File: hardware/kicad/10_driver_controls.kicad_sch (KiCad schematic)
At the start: 38 parts, among them J1001 DRIVER_CONTROLS, U1001 PC817 (safety-loop sense)

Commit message: sem-motor-controller v0.3: vehicle-interface provenance, transport-neutral core, clock trees, schematic checks
Provenance: the Cornell repositories are reference projects. Every place
that treated CHUDS / CAN FD / its VCU / 40 MHz as our vehicle is relabelled
or corrected (docs/PROVENANCE_AUDIT.md); the v0.2 checkpoint is preserved
with an errata banner.

Firmware: the core is transport-neutral (mc_core_on_msg_rx /
mc_core_msg_tx_poll / mc_core_on_link_state). CAN is one binding
(src/transport/mc_can_binding.c) whose 64-identifier block base is the new
calibration parameter supervision.can_id_base (id 164, rule 40, null in the
unconfigured config). ADR-0012. Tests: block relocation with a full ECO
engagement at 0x500, neutral API, rule-40 C/Python parity.

Clocking: tools/clock_tree.py evaluates 28 complete clock trees x 4 bus
cases from ST register widths and HAL ranges; the v0.2 "40 MHz required"
claim is withdrawn and the crystal is unselected until the bus is known.

Schematic: INA228 pins renumbered (KiCad-library cross-check, secondary);
DRV8353S stays an explicit placeholder; crystal unselected; PWR_FLAGs added
after a new pin-type check (not an ERC) found 6 undriven-rail errors.
Real KiCad ERC not run (KiCad 7 has no CLI ERC; tools/run_kicad_erc.sh).

Telematics: combined architecture with the STM32U575 / CAN 2.0B / LTE-MQTT
proposal (supervisor and CSIA placement, torque-request and driver-
authorization paths, pit/cloud outside the control chain), interface
difference table, generated DBC, logging-capacity and auxiliary-power
budget. Validation language separates command ceilings, envelope ramp,
phase current and battery current. CSIA: component attribution and a
next-evaluation plan; frozen results unchanged, nothing re-run.

Verified on the host: ctest 6/6 (4,006 checks), pytest 199 passed,
ARM core build 0 warnings, generators current, KiCad connectivity 0
problems. Nothing on hardware.

Co-Authored-By: Claude Opus 5.5 <noreply@anthropic.com>
Claude-Ses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
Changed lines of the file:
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@@
     (pin "2")
   )
-  (symbol (lib_id "Device:R") (at 248.92000000000002 66.04 0) (unit 1)
-    (in_bom yes) (on_board yes)
-    (property "Reference" "R1002" (id 0) (at 248.92000000000002 60.96000000000001 0)
-      (effects (font (size 1.27 1.27)))
-    )
-    (property "Value" "18k" (id 1) (at 248.92000000000002 71.12 0)
-      (effects (font (size 1.27 1.27)))
-    )
-    (property "Footprint" "" (id 2) (at 248.92000000000002 66.04 0)
-      (effects (font (size 1.27 1.27)) hide)
-    )
-    (property "Datasheet" "" (id 3) (at 248.92000000000002 66.04 0)
-      (effects (font (size 1.27 1.27)) hide)
-    )
-    (property "Status" "design value" (id 4) (at 248.92000000000002 66.04 0)
-      (effects (font (size 1.27 1.27)) hide)
-    )
-    (property "Rating_basis" "5 V -> 3.21 V" (id 5) (at 248.92000000000002 66.04 0)
+  (symbol (lib_id "Device:R") (at 248.92 66.04 0) (unit 1)
+    (in_bom yes) (on_board yes)
+    (property "Reference" "R1002" (id 0) (at 248.92 60.96000000000001 0)
+      (effects (font (size 1.27 1.27)))
+    )
+    (property "Value" "18k" (id 1) (at 248.92 71.12 0)
+      (effects (font (size 1.27 1.27)))
+    )
+    (property "Footprint" "" (id 2) (at 248.92 66.04 0)
+      (effects (font (size 1.27 1.27)) hide)
+    )
+    (property "Datasheet" "" (id 3) (at 248.92 66.04 0)
+      (effects (font (size 1.27 1.27)) hide)
+    )
+    (property "Status" "design value" (id 4) (at 248.92 66.04 0)
+      (effects (font (size 1.27 1.27)) hide)
+    )
+    (property "Rating_basis" "5 V -> 3.21 V" (id 5) (at 248.92 66.04 0)
       (effects (font (size 1.27 1.27)) hide)
     )
@@
     (pin "2")
   )
-  (symbol (lib_id "Device:C") (at 370.84000000000003 66.04 0) (unit 1)
-    (in_bom yes) (on_board yes)
-    (property "Reference" "C1001" (id 0) (at 370.84000000000003 60.96000000000001 0)
-      (effects (font (size 1.27 1.27)))
-    )
-    (property "Value" "100nF" (id 1) (at 370.84000000000003 71.12 0)
-      (effects (font (size 1.27 1.27)))
-    )
-    (property "Footprint" "" (id 2) (at 370.84000000000003 66.04 0)
-      (effects (font (size 1.27 1.27)) hide)
-    )
-    (property "Datasheet" "" (id 3) (at 370.84000000000003 66.04 0)
-      (effects (font (size 1.27 1.27)) hide)
-    )
-    (property "Status" "design value" (id 4) (at 370.84000000000003 66.04 0)
+  (symbol (lib_id "Device:C") (at 370.84 66.04 0) (unit 1)
+    (in_bom yes) (on_board yes)
+    (property "Reference" "C1001" (id 0) (at 370.84 60.96000000000001 0)
+      (effects (font (size 1.27 1.27)))
+    )
+    (property "Value" "100nF" (id 1) (at 370.84 71.12 0)
+      (effects (font (size 1.27 1.27)))
+    )
+    (property "Footprint" "" (id 2) (at 370.84 66.04 0)
+      (effects (font (size 1.27 1.27)) hide)
+    )
+    (property "Datasheet" "" (id 3) (at 370.84 66.04 0)
+      (effects (font (size 1.27 1.27)) hide)
+    )
+    (property "Status" "design value" (id 4) (at 370.84 66.04 0)
       (effects (font (size 1.27 1.27)) hide)
     )
@@
     (pin "2")
   )
-  (symbol (lib_id "Device:R") (at 248.92000000000002 119.38 0) (unit 1)
-    (in_bom yes) (on_board yes)
-    (property "Reference" "R1008" (id 0) (at 248.92000000000002 114.3 0)
-      (effects (font (size 1.27 1.27)))
-    )
-    (property "Value" "1k" (id 1) (at 248.92000000000002 124.46 0)
-      (effects (font (size 1.27 1.27)))
-    )
-    (property "Footprint" "" (id 2) (at 248.92000000000002 119.38 0)
-      (effects (font (size 1.27 1.27)) hide)
-    )
-    (property "Datasheet" "" (id 3) (at 248.92000000000002 119.38 0)
-      (effects (font (size 1.27 1.27)) hide)
-    )
-    (property "Status" "design value" (id 4) (at 248.92000000000002 119.38 0)
+  (symbol (lib_id "Device:R") (at 248.92 119.38 0) (unit 1)
+    (in_bom yes) (on_board yes)
+    (property "Reference" "R1008" (id 0) (at 248.92 114.3 0)
+      (effects (font (size 1.27 1.27)))
+    )
+    (property "Value" "1k" (id 1) (at 248.92 124.46 0)
+      (effects (font (size 1.27 1.27)))
+    )
+    (property "Footprint" "" (id 2) (at 248.92 119.38 0)
+      (effects (font (size 1.27 1.27)) hide)
+    )
+    (property "Datasheet" "" (id 3) (at 248.92 119.38 0)
+      (effects (font (size 1.27 1.27)) hide)
+    )
+    (property "Status" "design value" (id 4) (at 248.92 119.38 0)
       (effects (font (size 1.27 1.27)) hide)
     )
@@
     (pin "2")
   )
-  (symbol (lib_id "Device:R") (at 71.12 248.92000000000002 0) (unit 1)
-    (in_bom yes) (on_board yes)
-    (property "Reference" "R1020" (id 0) (at 71.12 243.84 0)
-      (effects (font (size 1.27 1.27)))
-    )
-    (property "Value" "10k" (id 1) (at 71.12 254.00000000000003 0)
-      (effects (font (size 1.27 1.27)))
-    )
-    (property "Footprint" "" (id 2) (at 71.12 248.92000000000002 0)
-      (effects (font (size 1.27 1.27)) hide)
-    )
-    (property "Datasheet" "" (id 3) (at 71.12 248.92000000000002 0)
-      (effects (font (size 1.27 1.27)) hide)
-    )
-    (property "Status" "design value" (id 4) (at 71.12 248.92000000000002 0)
-      (effects (font (size 1.27 1.27)) hide)
-    )
-    (property "Rating_basis" "HW_PERMIT low unless the loop is energised" (id 5) (at 71.12 248.92000000000002 0)
-      (effects (font (size 1.27 1.27)) hide)
-    )
-    (pin "1")
-    (pin "2")
-  )
-  (symbol (lib_id "Device:C") (at 129.54 248.92000000000002 0) (unit 1)
-    (in_bom yes) (on_board yes)
-    (property "Reference" "C1009" (id 0) (at 129.54 243.84 0)
-      (effects (font (size 1.27 1.27)))
-    )
-    (property "Value" "1nF" (id 1) (at 129.54 254.00000000000003 0)
-      (effects (font (size 1.27 1.27)))
-    )
-    (property "Footprint" "" (id 2) (at 129.54 248.92000000000002 0)
-      (effects (font (size 1.27 1.27)) hide)
-    )
-    (property "Datasheet" "" (id 3) (at 129.54 248.92000000000002 0)
-      (effects (font (size 1.27 1.27)) hide)
-    )
-    (property "Status" "design value" (id 4) (at 129.54 248.92000000000002 0)
-      (effects (font (size 1.27 1.27)) hide)
-    )
+  (symbol (lib_id "Device:R") (at 71.12 248.92 0) (unit 1)
+    (in_bom yes) (on_board yes)
+    (property "Reference" "R1020" (id 0) (at 71.12 243.83999999999997 0)
+      (effects (font (size 1.27 1.27)))
+    )
+    (property "Value" "10k" (id 1) (at 71.12 254.0 0)
+      (effects (font (size 1.27 1.27)))
+    )
+    (property "Footprint" "" (id 2) (at 71.12 248.92 0)
+      (effects (font (size 1.27 1.27)) hide)
+    )
+    (property "Datasheet" "" (id 3) (at 71.12 248.92 0)
+      (effects (font (size 1.27 1.27)) hide)
+    )
+    (property "Status" "design value" (id 4) (at 71.12 248.92 0)
+      (effects (font (size 1.27 1.27)) hide)
+    )
+    (property "Rating_basis" "HW_PERMIT low unless the loop is energised" (id 5) (at 71.12 248.92 0)
+      (effects (font (size 1.27 1.27)) hide)
+    )
+    (pin "1")
+    (pin "2")
+  )
+  (symbol (lib_id "Device:C") (at 129.54 248.92 0) (unit 1)
+    (in_bom yes) (on_board yes)
+    (property "Reference" "C1009" (id 0) (at 129.54 243.83999999999997 0)
+      (effects (font (size 1.27 1.27)))
+    )
+    (property "Value" "1nF" (id 1) (at 129.54 254.0 0)
+      (effects (font (size 1.27 1.27)))
+    )
+    (property "Footprint" "" (id 2) (at 129.54 248.92 0)
+      (effects (font (size 1.27 1.27)) hide)
+    )
+    (property "Datasheet" "" (id 3) (at 129.54 248.92 0)
+      (effects (font (size 1.27 1.27)) hide)
+    )
+    (property "Status" "design value" (id 4) (at 129.54 248.92 0)
+      (effects (font (size 1.27 1.27)) hide)
+    )

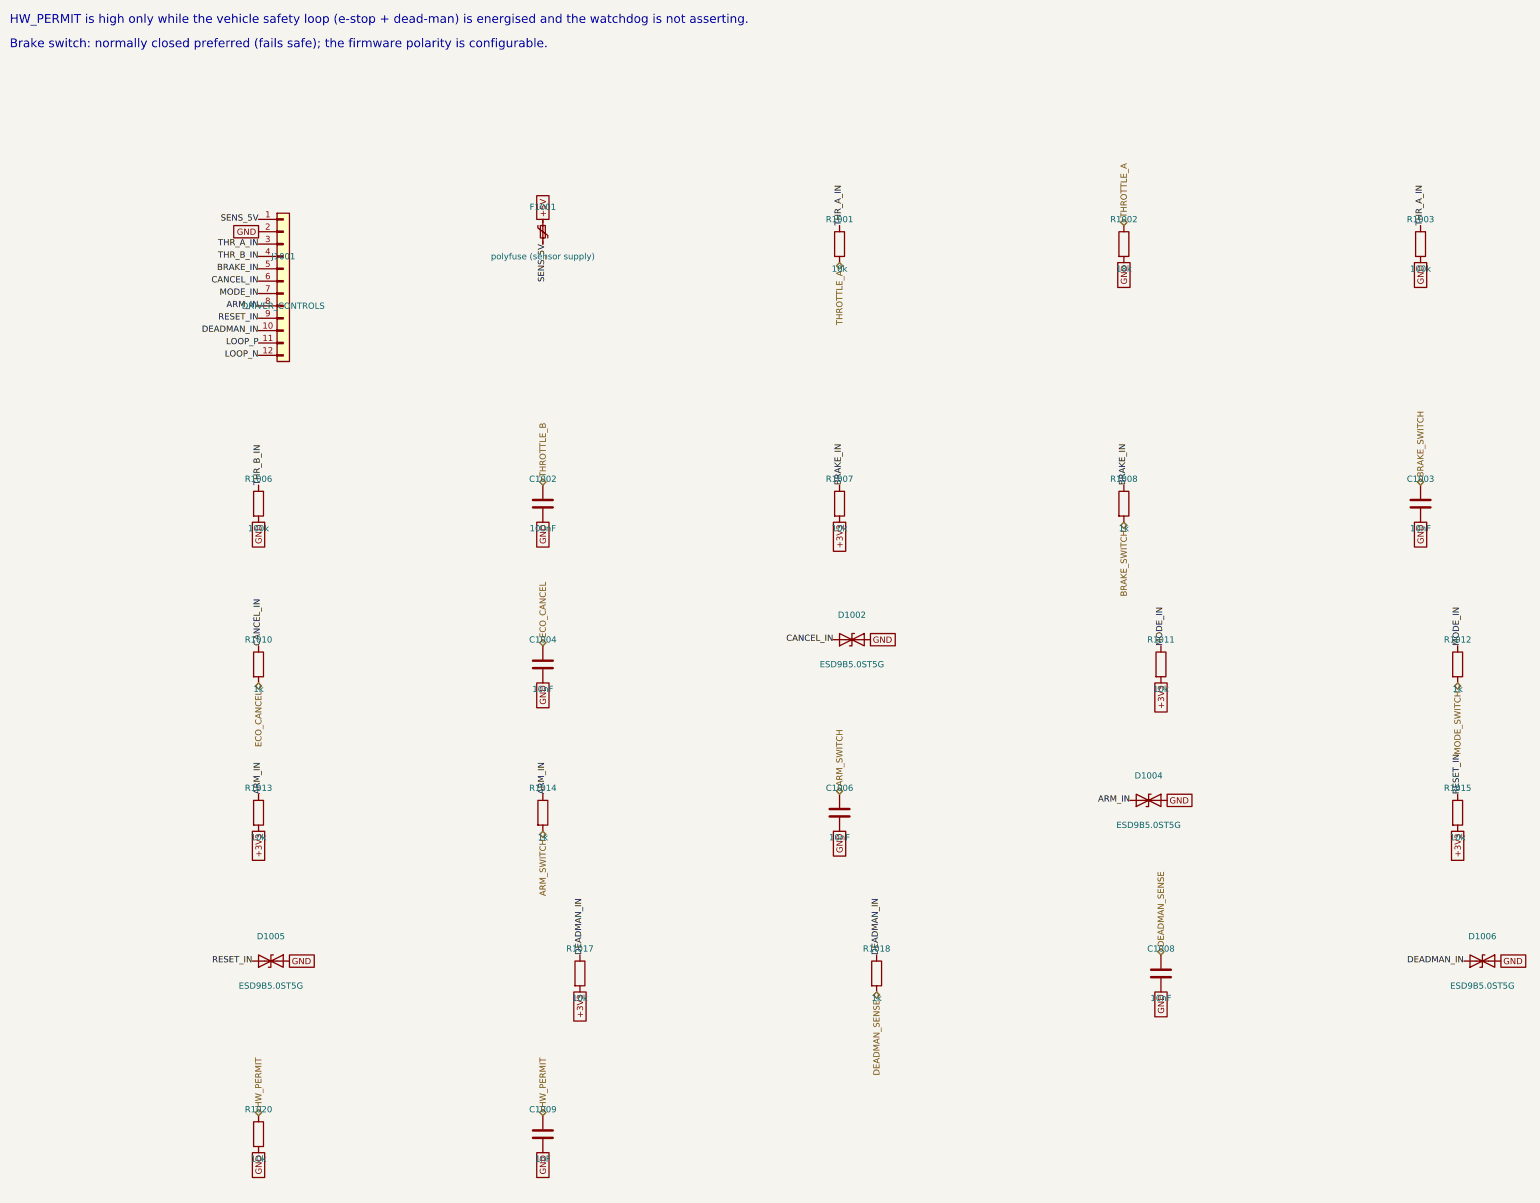
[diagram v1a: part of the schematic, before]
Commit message: hardware: design review, OV comparator hysteresis fix, test points, KiCad 8.0.9 libraries
hardware/review/DESIGN_REVIEW.md reviews the draft item by item (gate
driver, MOSFETs, DC link, current sensing, hardware overcurrent,
over/undervoltage, temperature, precharge, enable defaults and
watchdog, emergency interface, DC-DC, CAN, clock, debug and test
points) with an evidence level per statement, and records what each
open item needs.

Schematic changes that need no vehicle data:
- the over-voltage comparator's hysteresis resistor went straight onto
  the TL431 node, whose low impedance made the hysteresis undefined;
  the + input is now fed through 10 k and 390 k from the output sets
  -2.5 % / +0.8 % around the reference;
- the TL431 bias is 470 ohm (1.7 mA) instead of 1 k (0.8 mA), above
  its minimum cathode current (recalled; to confirm in the datasheet);
- the six pull-downs on the gate-signal inputs are fitted until the
  driver's own pull-downs are verified;
- 21 test points for the signals the acceptance procedures probe.
Connectivity: 136 intended nets, 0 problems; pin types 0 findings;
consistency 14 PASS, 4 OPEN.

The nine KiCad 8.0.9 ERC warnings were each compared with the library:
PWR_FLAG pin name, TL431 drawing, STM32G474 symbol geometry and the
NUP2105L datasheet URL changed between the 7.0.11 library the
schematic embedded and 8.0.9; no pin number, connected name, type or
net changed. The schematic is now generated from a pinned, SHA-256
checked copy of the 8.0.9 libraries (tools/fetch_kicad_symbols.py),
which the ERC also reads; KiCad 8's (hide yes) spelling is converted
for kiutils so no field becomes visible. Both CI jobs use KiCad 8.

Firmware: the brake switch type is a calibration value; a separate
bench image (semmc_stm32g474_pwmtest) switches the gate signals at
fixed duties with DRV_ENABLE held low for acceptance stage 4; g_bench
also reports the input states.

Co-Authored-By: Claude Opus 5.5 <noreply@anthropic.com>
Claude-Session: https:/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
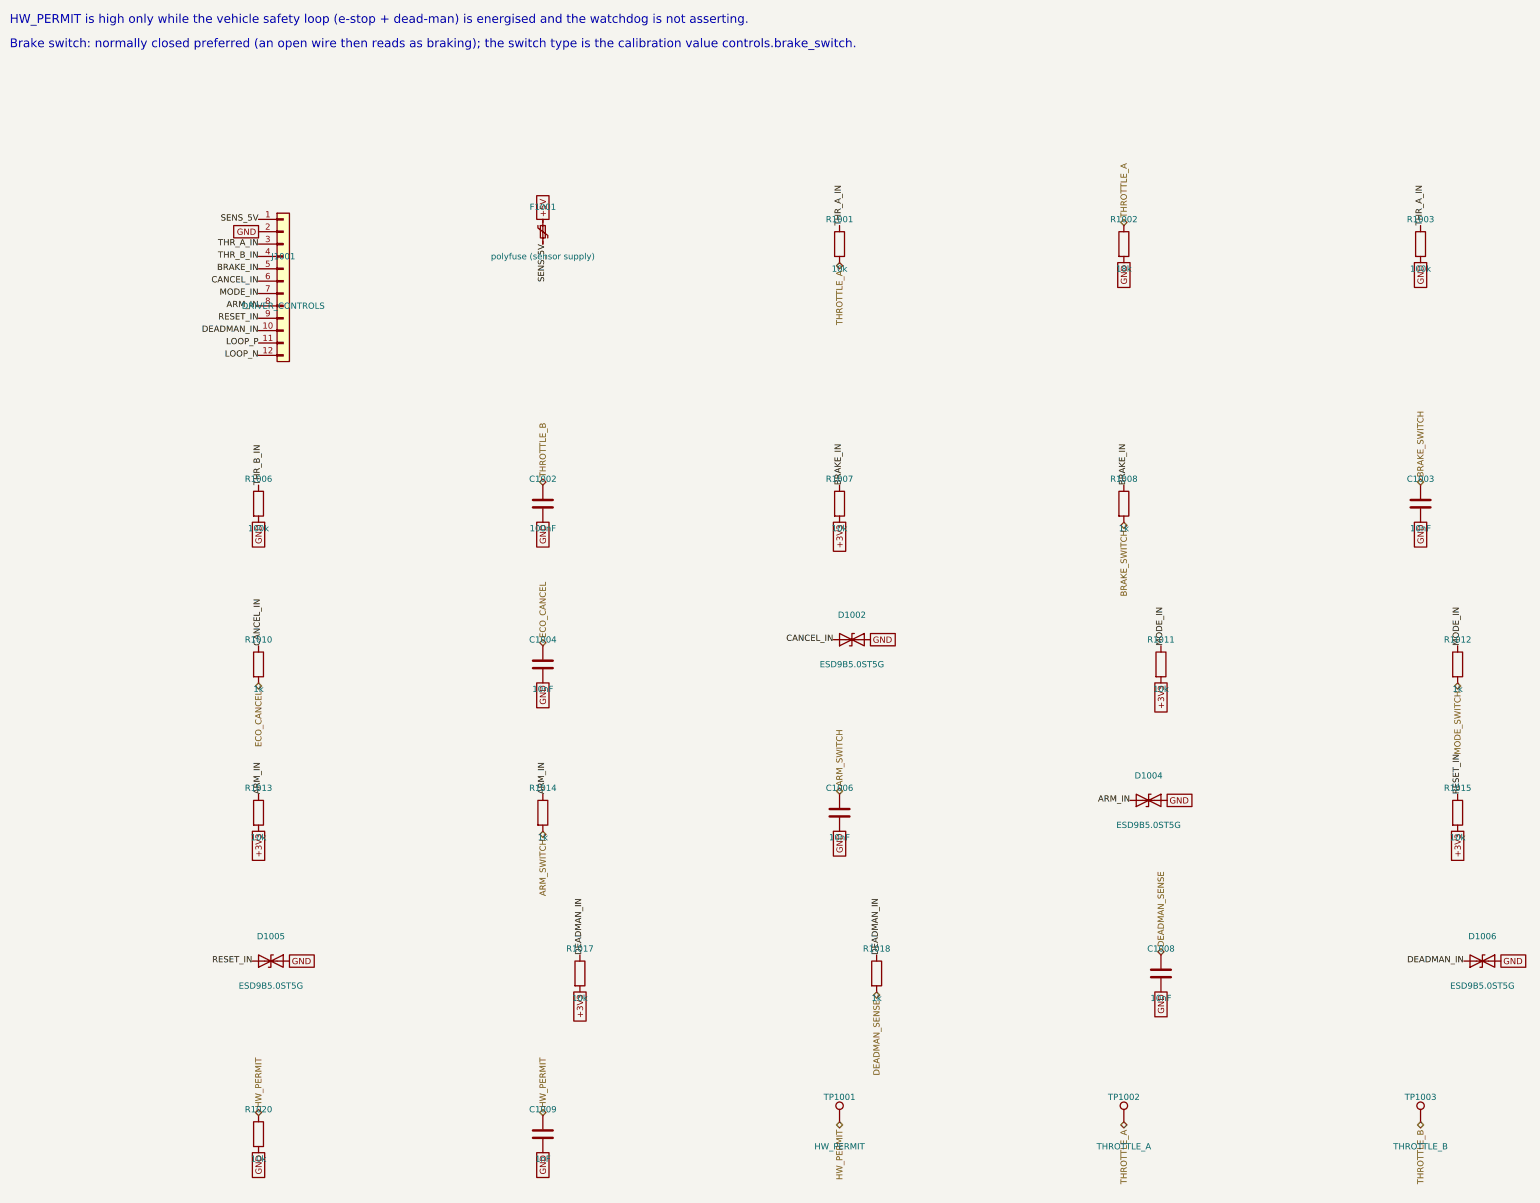
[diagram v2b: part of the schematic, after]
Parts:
- added TP1001: HW_PERMIT, symbol Connector:TestPoint
- added TP1002: THROTTLE_A, symbol Connector:TestPoint
- added TP1003: THROTTLE_B, symbol Connector:TestPoint
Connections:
- net HW_PERMIT: now also TP1001.1
- net THROTTLE_A: now also TP1002.1
- net THROTTLE_B: now also TP1003.1
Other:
- note added: "Brake switch: normally closed preferred (an open wire then reads as braking); the switch type is the calibration value controls.brake_switch."
- note removed: "Brake switch: normally closed preferred (fails safe); the firmware polarity is configurable."
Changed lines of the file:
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@@
     (effects (font (size 1.8 1.8)) (justify left))
   )
-  (text "Brake switch: normally closed preferred (fails safe); the firmware polarity is configurable."
+  (text "Brake switch: normally closed preferred (an open wire then reads as braking); the switch type is the calibration value controls.brake_switch."
     (at 20.0 25.0 0)
     (effects (font (size 1.8 1.8)) (justify left))
@@
   (hierarchical_label "HW_PERMIT" (shape bidirectional) (at 129.54 245.11 90)
     (effects (font (size 1.27 1.27)) (justify left))
+  )
+  (hierarchical_label "HW_PERMIT" (shape bidirectional) (at 190.5 246.38 270)
+    (effects (font (size 1.27 1.27)) (justify right))
+  )
+  (hierarchical_label "THROTTLE_A" (shape bidirectional) (at 248.92 246.38 270)
+    (effects (font (size 1.27 1.27)) (justify right))
+  )
+  (hierarchical_label "THROTTLE_B" (shape bidirectional) (at 309.88 246.38 270)
+    (effects (font (size 1.27 1.27)) (justify right))
   )
   (symbol (lib_id "Connector_Generic:Conn_01x12") (at 76.2 73.66 0) (unit 1)
@@
     (pin "2")
   )
+  (symbol (lib_id "Connector:TestPoint") (at 190.5 246.38 0) (unit 1)
+    (in_bom yes) (on_board yes)
+    (property "Reference" "TP1001" (id 0) (at 190.5 241.29999999999998 0)
+      (effects (font (size 1.27 1.27)))
+    )
+    (property "Value" "HW_PERMIT" (id 1) (at 190.5 251.46 0)
+      (effects (font (size 1.27 1.27)))
+    )
+    (property "Footprint" "" (id 2) (at 190.5 246.38 0)
+      (effects (font (size 1.27 1.27)) hide)
+    )
+    (property "Datasheet" "" (id 3) (at 190.5 246.38 0)
+      (effects (font (size 1.27 1.27)) hide)
+    )
+    (property "Status" "bench test point" (id 4) (at 190.5 246.38 0)
+      (effects (font (size 1.27 1.27)) hide)
+    )
+    (pin "1")
+  )
+  (symbol (lib_id "Connector:TestPoint") (at 248.92 246.38 0) (unit 1)
+    (in_bom yes) (on_board yes)
+    (property "Reference" "TP1002" (id 0) (at 248.92 241.29999999999998 0)
+      (effects (font (size 1.27 1.27)))
+    )
+    (property "Value" "THROTTLE_A" (id 1) (at 248.92 251.46 0)
+      (effects (font (size 1.27 1.27)))
+    )
+    (property "Footprint" "" (id 2) (at 248.92 246.38 0)
+      (effects (font (size 1.27 1.27)) hide)
+    )
+    (property "Datasheet" "" (id 3) (at 248.92 246.38 0)
+      (effects (font (size 1.27 1.27)) hide)
+    )
+    (property "Status" "bench test point" (id 4) (at 248.92 246.38 0)
+      (effects (font (size 1.27 1.27)) hide)
+    )
+    (pin "1")
+  )
+  (symbol (lib_id "Connector:TestPoint") (at 309.88 246.38 0) (unit 1)
+    (in_bom yes) (on_board yes)
+    (property "Reference" "TP1003" (id 0) (at 309.88 241.29999999999998 0)
+      (effects (font (size 1.27 1.27)))
+    )
+    (property "Value" "THROTTLE_B" (id 1) (at 309.88 251.46 0)
+      (effects (font (size 1.27 1.27)))
+    )
+    (property "Footprint" "" (id 2) (at 309.88 246.38 0)
+      (effects (font (size 1.27 1.27)) hide)
+    )
+    (property "Datasheet" "" (id 3) (at 309.88 246.38 0)
+      (effects (font (size 1.27 1.27)) hide)
+    )
+    (property "Status" "bench test point" (id 4) (at 309.88 246.38 0)
+      (effects (font (size 1.27 1.27)) hide)
+    )
+    (pin "1")
+  )
   (sheet_instances
